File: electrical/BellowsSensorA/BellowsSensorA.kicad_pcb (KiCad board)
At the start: 2 copper layers, 30 x 20 mm, 5 parts, among them J1 I2C, U1 ELVH-001D-HRRJ-C-N2A4

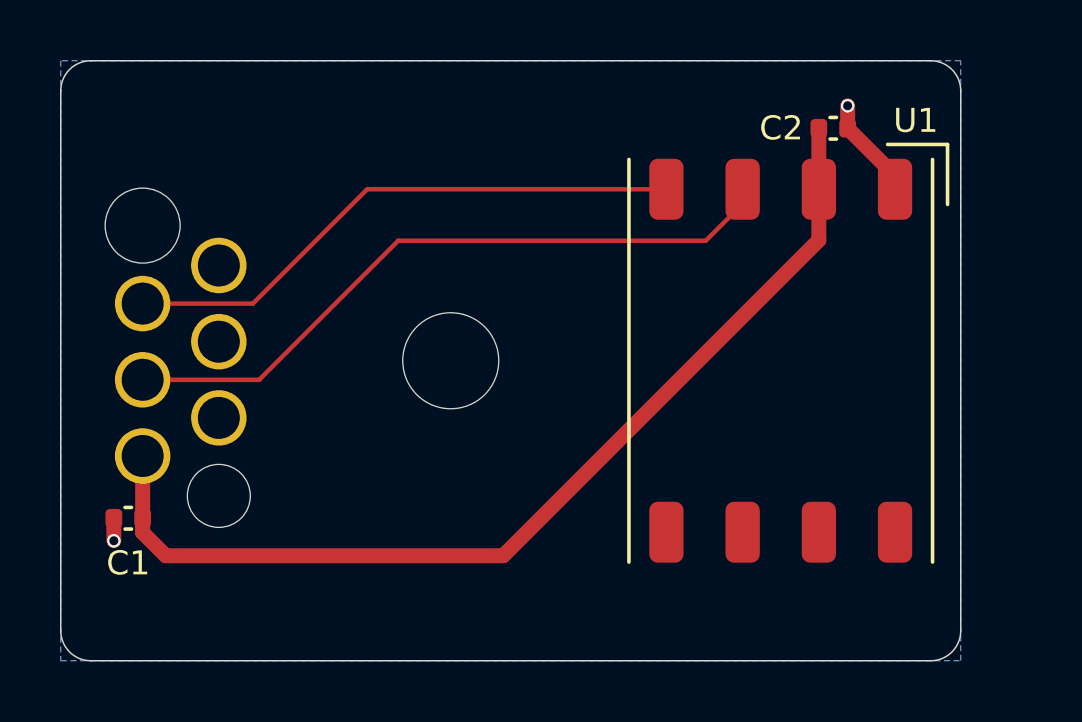
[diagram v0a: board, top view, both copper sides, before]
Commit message: Switch pressure sensor for BellowsSensorA
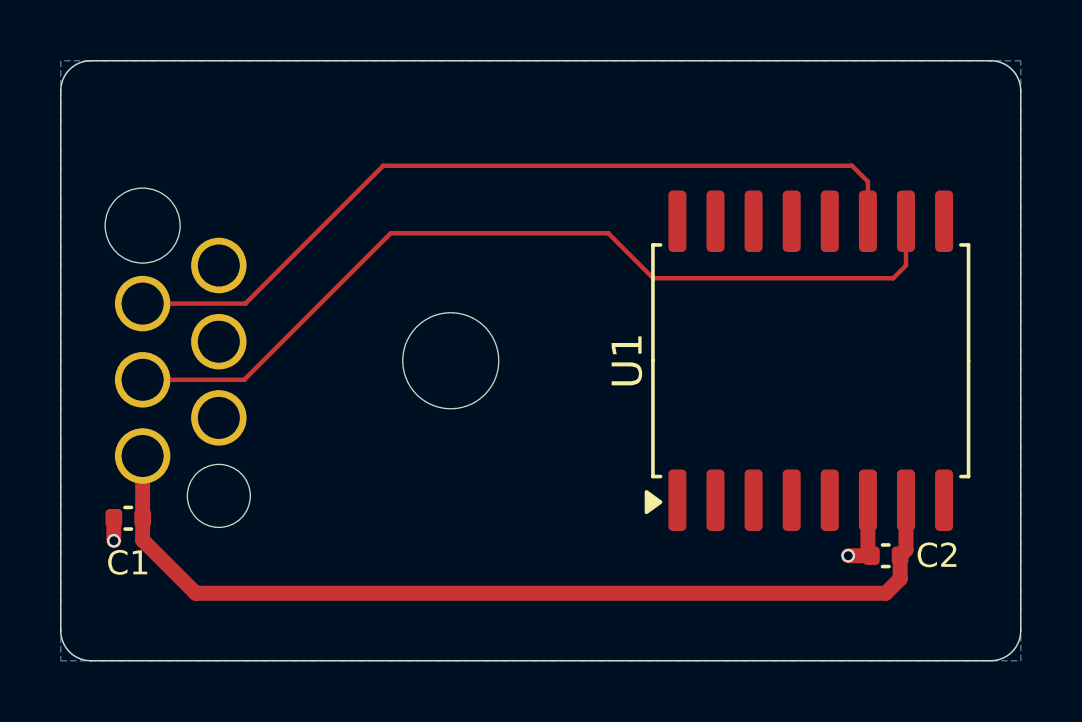
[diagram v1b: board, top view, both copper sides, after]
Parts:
- U1: value ELVH-001D-HRRJ-C-N2A4 -> CPS610DSD010DH01; footprint MidiConcertina:Amphenol_ELVH-x-xJ-x-x -> Package_SO:SOIC-16W_7.5x10.3mm_P1.27mm
- moved C2 14.4 mm to (155.5, 110.5), turned to 180 degrees
- moved U1 1.00 mm to (153.0, 104.0), turned to 90 degrees
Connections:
- U1 pad 1: GND -> unconnected-(U1-Pad1)
- U1 pad 2: +3.3V -> unconnected-(U1-Pad2)
- U1 pad 3: /I2C_SDA -> unconnected-(U1-Pad3)
- U1 pad 4: /I2C_SCL -> unconnected-(U1-Pad4)
- U1 pad 6: unconnected-(U1-NC-Pad6) -> GND
- U1 pad 7: unconnected-(U1-NC-Pad7) -> +3.3V
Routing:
- net /I2C_SCL: track 19.0 -> 27.6 mm
- net /I2C_SDA: track 22.9 -> 29.7 mm
- net +3.3V: track 33.5 -> 31.7 mm
- net GND: track 4.19 -> 3.42 mm
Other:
- board size 30 x 20 mm -> 32 x 20 mm
